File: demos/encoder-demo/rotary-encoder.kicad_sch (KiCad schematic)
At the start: 9 parts, among them SW1 RotaryEncoder

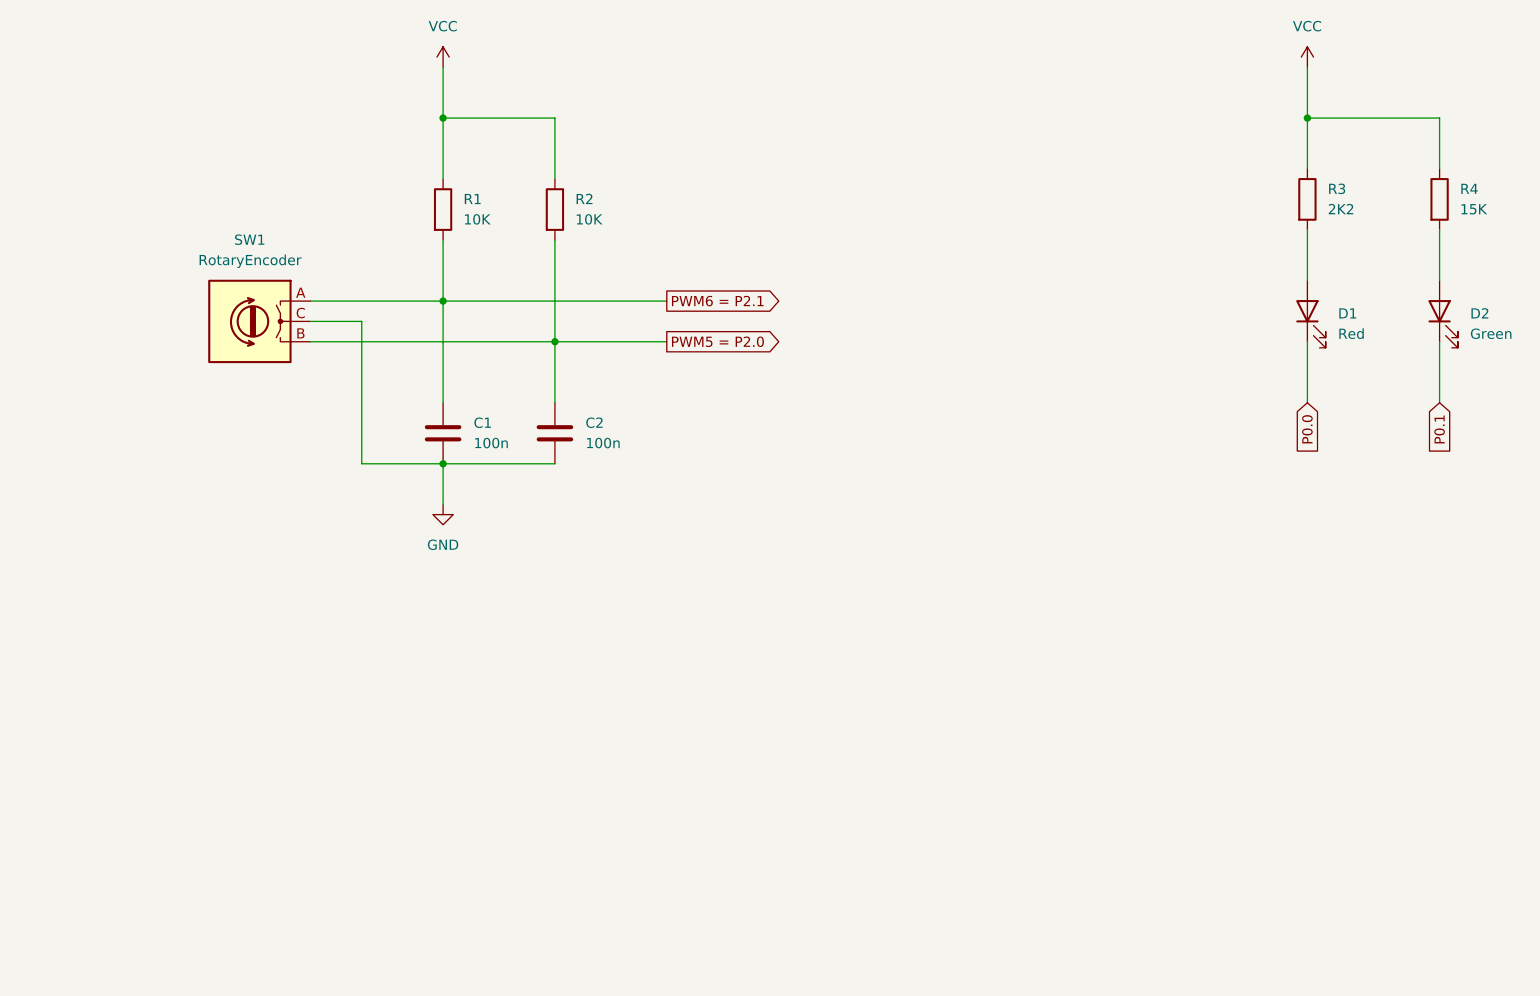
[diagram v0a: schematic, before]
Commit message: Updated encoder demo
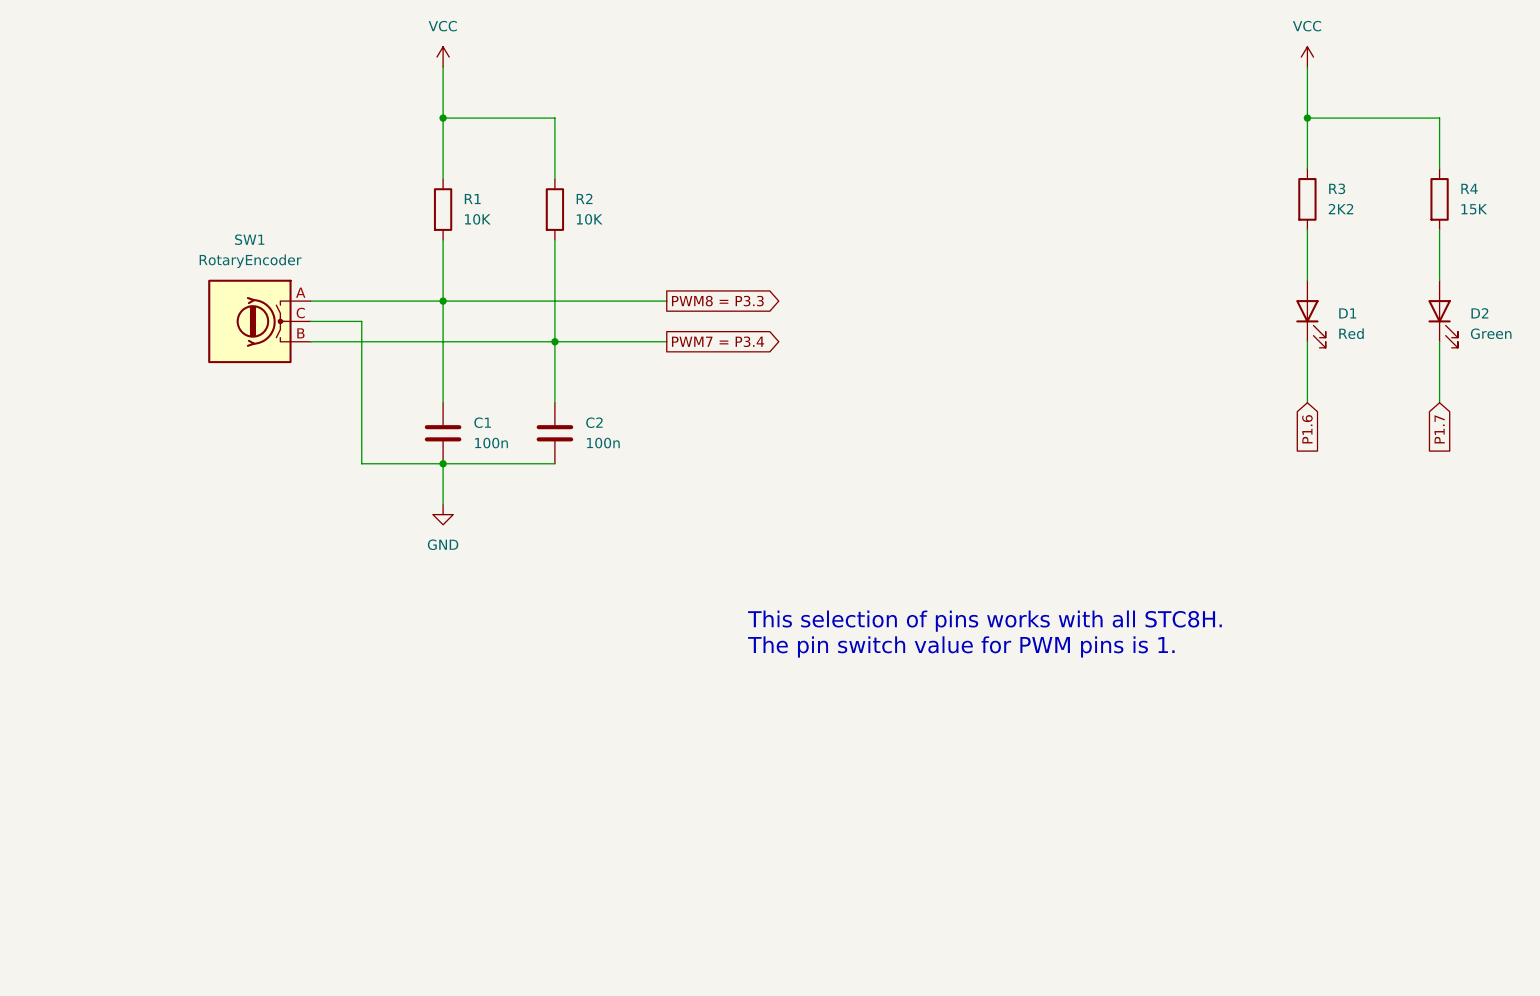
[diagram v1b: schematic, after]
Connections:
- net P0.0 renamed P1.6
- net P0.1 renamed P1.7
- net PWM5 = P2.0 renamed PWM7 = P3.4
- net PWM6 = P2.1 renamed PWM8 = P3.3
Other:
- note added: "This selection of pins works with all STC8H. The pin switch value for PWM pins is 1."

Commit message: Updated schematic
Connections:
- net P1.6 renamed P3.6
- net P1.7 renamed P3.7
- net PWM7 = P3.4 renamed B
- net PWM8 = P3.3 renamed A
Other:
- note added: "Counter | Encoder A | Encoder B | Pin switch ---------+--------------+--------------+------------ A | PWM1P = P1.0 | PWM2P = P1.2 | 0 B | PWM5 = P1.7 | PWM6 = P5.4 | 1 Note: on the STC8H4 and STC8H8, PWM2P is on P5.4 instead of P1.2."
- note removed: "This selection of pins works with all STC8H. The pin switch value for PWM pins is 1."
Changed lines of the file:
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@@
     (stroke (width 0) (type default))
   )
-  (text "This selection of pins works with all STC8H.\nThe pin switch value for PWM pins is 1."
-    (at 132.08 138.43 0)
-    (effects (font (size 2 2)) (justify left bottom))
+  (text " Counter |  Encoder A   |  Encoder B   | Pin switch\n---------+--------------+--------------+------------\n    A    | PWM1P = P1.0 | PWM2P = P1.2 |     0\n    B    | PWM5  = P1.7 | PWM6  = P5.4 |     1\n\nNote: on the STC8H4 and STC8H8, PWM2P is on P5.4 \ninstead of P1.2."
+    (at 40.64 177.8 0)
+    (effects (font (face "Noto Sans Mono") (size 2.54 2.54)) (justify left bottom))
   )
-  (global_label "P1.7" (shape input) (at 218.44 106.68 270) (fields_autoplaced)
+  (global_label "P3.7" (shape input) (at 218.44 106.68 270) (fields_autoplaced)
     (effects (font (size 1.27 1.27)) (justify right))
     (property "Intersheetrefs" "${INTERSHEET_REFS}" (at 218.44 113.8796 90)
@@
     )
   )
-  (global_label "P1.6" (shape input) (at 201.93 106.68 270) (fields_autoplaced)
+  (global_label "P3.6" (shape input) (at 201.93 106.68 270) (fields_autoplaced)
     (effects (font (size 1.27 1.27)) (justify right))
     (property "Intersheetrefs" "${INTERSHEET_REFS}" (at 201.93 113.8796 90)
@@
     )
   )
-  (global_label "PWM7 = P3.4" (shape output) (at 121.92 99.06 0) (fields_autoplaced)
+  (global_label "B" (shape output) (at 121.92 99.06 0) (fields_autoplaced)
     (effects (font (size 1.27 1.27)) (justify left))
-    (property "Intersheetrefs" "${INTERSHEET_REFS}" (at 138.0095 99.06 0)
+    (property "Intersheetrefs" "${INTERSHEET_REFS}" (at 126.0958 99.06 0)
       (effects (font (size 1.27 1.27)) (justify left) hide)
     )
   )
-  (global_label "PWM8 = P3.3" (shape output) (at 121.92 93.98 0) (fields_autoplaced)
+  (global_label "A" (shape output) (at 121.92 93.98 0) (fields_autoplaced)
     (effects (font (size 1.27 1.27)) (justify left))
-    (property "Intersheetrefs" "${INTERSHEET_REFS}" (at 138.0095 93.98 0)
+    (property "Intersheetrefs" "${INTERSHEET_REFS}" (at 125.9144 93.98 0)
       (effects (font (size 1.27 1.27)) (justify left) hide)
     )
